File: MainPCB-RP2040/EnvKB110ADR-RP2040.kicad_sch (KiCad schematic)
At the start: 285 parts, among them J2 EVQPU, J5 Conn_01x03_Male, U1 TLV75533PDBVR, U3 RP2040, Y1 3225_4P

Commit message: added missing stabilizers and updated gerber
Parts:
- added stab7, stab8, stab9: MountingHole, Mounting_Keyboard_Stabilizer:Stabilizer_Cherry_MX_2u, symbol Mechanical:MountingHole
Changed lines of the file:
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@@
+    )
+  )
+  (symbol (lib_id "Mechanical:MountingHole") (at 110.49 284.48 0) (unit 1)
+    (in_bom yes) (on_board yes)
+    (property "Reference" "stab8" (id 0) (at 113.03 283.3116 0)
+      (effects (font (size 1.27 1.27)) (justify left))
+    )
+    (property "Value" "MountingHole" (id 1) (at 113.03 285.623 0)
+      (effects (font (size 1.27 1.27)) (justify left))
+    )
+    (property "Footprint" "Mounting_Keyboard_Stabilizer:Stabilizer_Cherry_MX_2u" (id 2) (at 110.49 284.48 0)
+      (effects (font (size 1.27 1.27)) hide)
+    )
+    (property "Datasheet" "~" (id 3) (at 110.49 284.48 0)
+      (effects (font (size 1.27 1.27)) hide)
+    )
+  )
+  (symbol (lib_id "Mechanical:MountingHole") (at 110.49 280.67 0) (unit 1)
+    (in_bom yes) (on_board yes)
+    (property "Reference" "stab7" (id 0) (at 113.03 279.5016 0)
+      (effects (font (size 1.27 1.27)) (justify left))
+    )
+    (property "Value" "MountingHole" (id 1) (at 113.03 281.813 0)
+      (effects (font (size 1.27 1.27)) (justify left))
+    )
+    (property "Footprint" "Mounting_Keyboard_Stabilizer:Stabilizer_Cherry_MX_2u" (id 2) (at 110.49 280.67 0)
+      (effects (font (size 1.27 1.27)) hide)
+    )
+    (property "Datasheet" "~" (id 3) (at 110.49 280.67 0)
+      (effects (font (size 1.27 1.27)) hide)
+    )
+  )
+  (symbol (lib_id "Mechanical:MountingHole") (at 110.49 288.29 0) (unit 1)
+    (in_bom yes) (on_board yes)
+    (property "Reference" "stab9" (id 0) (at 113.03 287.1216 0)
+      (effects (font (size 1.27 1.27)) (justify left))
+    )
+    (property "Value" "MountingHole" (id 1) (at 113.03 289.433 0)
+      (effects (font (size 1.27 1.27)) (justify left))
+    )
+    (property "Footprint" "Mounting_Keyboard_Stabilizer:Stabilizer_Cherry_MX_2u" (id 2) (at 110.49 288.29 0)
+      (effects (font (size 1.27 1.27)) hide)
+    )
+    (property "Datasheet" "~" (id 3) (at 110.49 288.29 0)
+      (effects (font (size 1.27 1.27)) hide)
     )
   )
@@
       (reference "stab6") (unit 1) (value "MountingHole") (footprint "Mounting_Keyboard_Stabilizer:Stabilizer_Cherry_MX_2u")
     )
+    (path "/94062c5c-0205-48cd-835d-0cc87df473b9"
+      (reference "stab7") (unit 1) (value "MountingHole") (footprint "Mounting_Keyboard_Stabilizer:Stabilizer_Cherry_MX_2u")
+    )
+    (path "/88476138-3ded-4644-b39d-e4e08664e937"
+      (reference "stab8") (unit 1) (value "MountingHole") (footprint "Mounting_Keyboard_Stabilizer:Stabilizer_Cherry_MX_2u")
+    )
+    (path "/cfc7fa23-12c8-423d-a92d-1a89c9edd662"
+      (reference "stab9") (unit 1) (value "MountingHole") (footprint "Mounting_Keyboard_Stabilizer:Stabilizer_Cherry_MX_2u")
+    )
   )

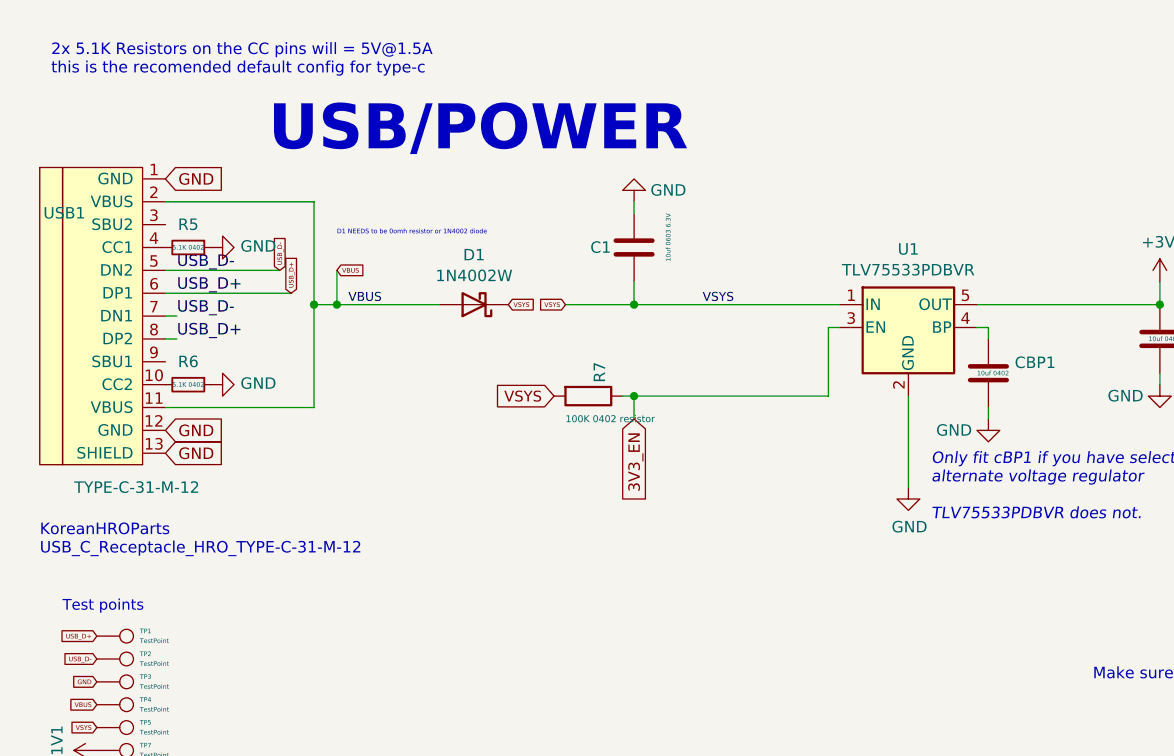
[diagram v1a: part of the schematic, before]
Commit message: swapped port for mid-mount version
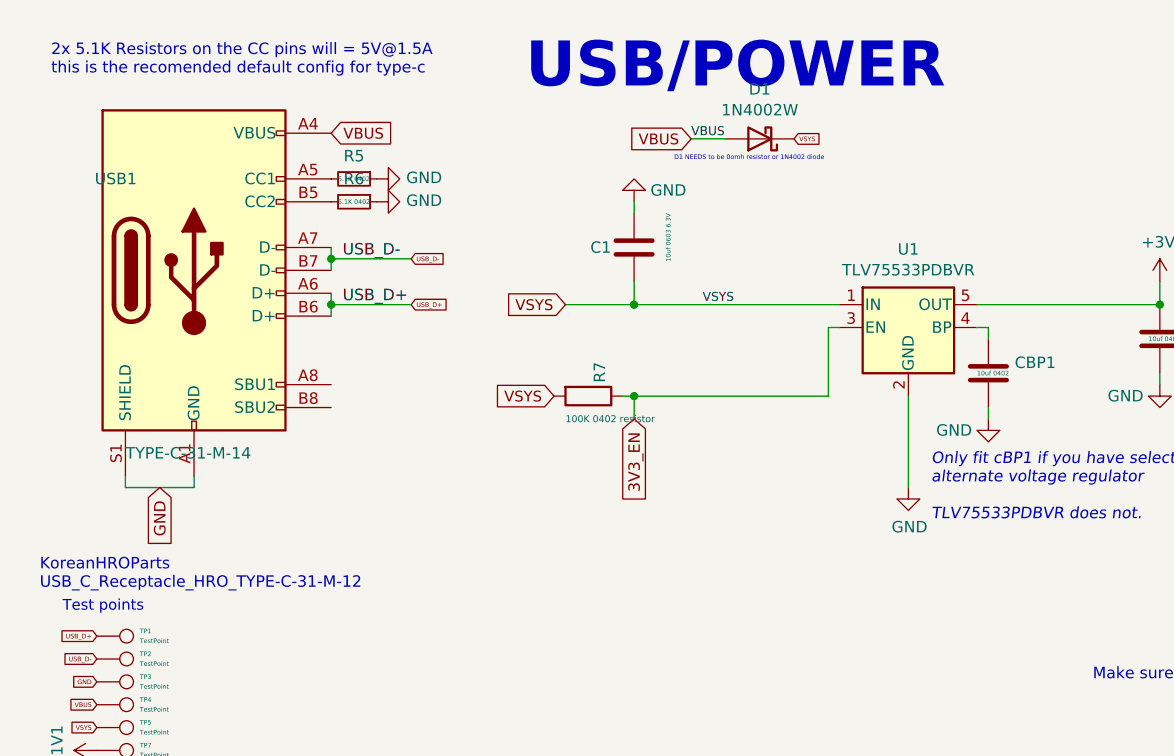
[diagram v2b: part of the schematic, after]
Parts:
- USB1: value TYPE-C-31-M-12 -> TYPE-C-31-M-14; footprint HRO-TYPE-C31-M-12:HRO-TYPE-C-31-M-12 -> josh-connectors:USB_C_TYPE-C-31-M-14; symbol Type-C:HRO-TYPE-C-31-M-12 -> josh-connector:USB_C_U262-161N-4BVC11; LCSC C165948 -> C319148; MPN (none) -> U262-161N-4BVC11; Manufacturer (none) -> XKB Enterprise
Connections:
- net GND: now also USB1.A1 (GND), USB1.A12 (GND), USB1.B1 (GND), USB1.B12 (GND), USB1.S1 (SHIELD); no longer USB1.1 (GND), USB1.12 (GND), USB1.13 (SHIELD)
- net USB_D+: now also USB1.A6 (D+), USB1.B6 (D+); no longer USB1.6 (DP1), USB1.8 (DP2)
- net USB_D-: now also USB1.A7 (D-), USB1.B7 (D-); no longer USB1.5 (DN2), USB1.7 (DN1)
- net VBUS: now also USB1.A4 (VBUS), USB1.A9 (VBUS), USB1.B4 (VBUS), USB1.B9 (VBUS); no longer USB1.11 (VBUS), USB1.2 (VBUS)
- net at R6.2: now also USB1.B5 (CC2); no longer USB1.10 (CC2)
- net at R5.2: now also USB1.A5 (CC1); no longer USB1.4 (CC1)
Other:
- moved on the sheet: D1, R5, R6

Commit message: Added part number for the nor flash and also changed footprint to correct one? also added some smol easter eggs.
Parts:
- FLASH1: value W25Q16 -> W25Q16JVSSIQ; footprint Package_SO:SOIC-8_5.275x5.275mm_P1.27mm -> Package_SO:SOIC-8W_5.3x5.3mm_P1.27mm
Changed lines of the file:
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@@
     (in_bom yes) (on_board yes)
     (property "Reference" "FLASH1" (id 0) (at 78.74 133.35 0))
-    (property "Value" "W25Q16" (id 1) (at 78.74 146.05 0))
-    (property "Footprint" "Package_SO:SOIC-8_5.275x5.275mm_P1.27mm" (id 2) (at 78.74 133.35 0)
+    (property "Value" "W25Q16JVSSIQ" (id 1) (at 78.74 146.05 0))
+    (property "Footprint" "Package_SO:SOIC-8W_5.3x5.3mm_P1.27mm" (id 2) (at 78.74 133.35 0)
       (effects (font (size 1.27 1.27)) (justify left bottom) hide)
     )
@@
     )
     (path "/00000000-0000-0000-0000-0000608edada"
-      (reference "FLASH1") (unit 1) (value "W25Q16") (footprint "Package_SO:SOIC-8_5.275x5.275mm_P1.27mm")
+      (reference "FLASH1") (unit 1) (value "W25Q16JVSSIQ") (footprint "Package_SO:SOIC-8W_5.3x5.3mm_P1.27mm")
     )
     (path "/00000000-0000-0000-0000-000060ccb1e5"

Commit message: various improvements/ made ISO only (for now maybe)
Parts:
- C1: value 10uf 0603 6.3V -> (none); footprint Capacitor_SMD:C_0603_1608Metric -> (none)
- C10, C3: value 1uf 0402 -> (none); footprint Capacitor_SMD:C_0402_1005Metric -> (none)
- C11, C13, C14, C15, C16, C18, C5, C6, C7, C8: value 100nf 0402 -> (none); footprint Capacitor_SMD:C_0402_1005Metric -> (none)
- C17, C4, CBP1: value 10uf 0402 -> (none); footprint Capacitor_SMD:C_0402_1005Metric -> (none)
- C19, C2: value 22pf 0402 -> (none); footprint Capacitor_SMD:C_0402_1005Metric -> (none)
- D1: value 1N4002W -> (none); footprint Diode_SMD:D_SOD-123 -> (none)
- D3: value LED_0603 -> (none); footprint LED_SMD:LED_0603_1608Metric -> (none)
- D_100, D_101, D_102, D_103, D_104, D_105, D_106, D_107, D_108, D_109, D_110, D_111, D_112, D_113, D_114, D_115, D_116, D_12, D_13, D_14, D_15, D_16, D_17, D_18, D_19, D_20, D_21, D_22, D_23, D_24, D_25, D_26, D_27, D_28, D_29, D_30, D_31, D_32, D_33, D_34, D_35, D_36, D_37, D_38, D_39, D_40, D_41, D_42, D_43, D_44, D_45, D_46, D_47, D_48, D_49, D_50, D_51, D_52, D_53, D_54, D_55, D_56, D_57, D_58, D_59, D_60, D_61, D_62, D_63, D_64, D_65, D_66, D_67, D_68, D_69, D_70, D_71, D_72, D_73, D_74, D_75, D_76, D_77, D_78, D_79, D_80, D_81, D_82, D_83, D_84, D_85, D_86, D_87, D_88, D_89, D_90, D_91, D_92, D_93, D_94, D_95, D_96, D_97, D_98, D_99, D_ANSI_1: value SOD-123 -> (none); footprint Diode_SMD:D_SOD-123 -> (none)
- FLASH1: value W25Q16JVSSIQ -> (none); footprint Package_SO:SOIC-8W_5.3x5.3mm_P1.27mm -> (none)
- H1, H10, H11, H12, H13, H14, H15, H16, H17, H18, H2, H3, H4, H5, H6, H7, H8, H9: value MountingHole -> (none); footprint MountingHole:MountingHole_2.2mm_M2_Pad -> (none)
- J2, RSW1: value EVQPU -> (none); footprint Button_Switch_SMD:Panasonic_EVQPUJ_EVQPUA -> (none)
- J5: value Conn_01x03_Male -> (none); footprint Connector_PinHeader_2.54mm:PinHeader_1x03_P2.54mm_Horizontal -> (none)
- K_100, K_101, K_102, K_103, K_104, K_105, K_106, K_107, K_108, K_109, K_110, K_111, K_112, K_113, K_114, K_115, K_116, K_12, K_13, K_14, K_15, K_16, K_17, K_18, K_19, K_20, K_21, K_22, K_23, K_24, K_25, K_26, K_27, K_28, K_29, K_30, K_31, K_32, K_33, K_34, K_35, K_36, K_37, K_38, K_39, K_40, K_41, K_42, K_43, K_44, K_45, K_46, K_47, K_48, K_49, K_50, K_51, K_52, K_53, K_54, K_55, K_56, K_57, K_58, K_59, K_60, K_61, K_62, K_63, K_64, K_65, K_66, K_67, K_68, K_69, K_70, K_71, K_72, K_73, K_74, K_75, K_76, K_77, K_78, K_79, K_80, K_81, K_82, K_83, K_84, K_85, K_86, K_87, K_88, K_89, K_90, K_91, K_92, K_93, K_94, K_95, K_96, K_97, K_98, K_99, K_ANSI_1, K_ANSI_2, K_ANSI_3: value KEYSW -> (none); footprint MX_Only:MXOnly-1U-Hotswap-custom -> (none)
- PWRLED1: value LED_0805 -> (none); footprint LED_SMD:LED_0805_2012Metric -> (none)
- R1, R11: value 1K 0402 Resistor -> (none); footprint Capacitor_SMD:C_0402_1005Metric -> (none)
- R12: value 1K 0402 Resistor -> (none); footprint Resistor_SMD:R_0402_1005Metric -> (none)
- R2: value 10K 0402 -> (none); footprint Capacitor_SMD:C_0402_1005Metric -> (none)
- R3, R4: value 27 0402 Resistor -> (none); footprint Resistor_SMD:R_0402_1005Metric -> (none)
- R5, R6: value 5.1K 0402 -> (none); footprint Resistor_SMD:R_0402_1005Metric -> (none)
- R7: value 100K 0402 resistor -> (none); footprint Resistor_SMD:R_0402_1005Metric -> (none)
- R8: value 470 0402 Resistor -> (none); footprint Resistor_SMD:R_0402_1005Metric -> (none)
- TP1, TP2, TP3, TP4, TP5, TP6, TP7, TP8: value TestPoint -> (none); footprint TestPoint:TestPoint_Pad_D1.0mm -> (none)
- U1: value TLV75533PDBVR -> (none); footprint Package_TO_SOT_SMD:SOT-23-5 -> (none)
- U3: value RP2040 -> (none); footprint RP2040_minimal:RP2040-QFN-56 -> (none)
- USB1: value TYPE-C-31-M-14 -> (none); footprint josh-connectors:USB_C_TYPE-C-31-M-14 -> (none)
- Y1: value 3225_4P -> (none); footprint Crystal:Crystal_SMD_3225-4Pin_3.2x2.5mm -> (none)
- stab1, stab2, stab3, stab4, stab6, stab7, stab8, stab9: value MountingHole -> (none); footprint Mounting_Keyboard_Stabilizer:Stabilizer_Cherry_MX_2u -> (none)
- stab5: value MountingHole -> (none); footprint Mounting_Keyboard_Stabilizer:Stabilizer_Cherry_MX_6.25u -> (none)

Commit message: properly implemented ANSI/ISO support.
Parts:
- C1: value (none) -> 10uf 0603 6.3V; footprint (none) -> Capacitor_SMD:C_0603_1608Metric
- C10, C3: value (none) -> 1uf 0402; footprint (none) -> Capacitor_SMD:C_0402_1005Metric
- C11, C13, C14, C15, C16, C18, C5, C6, C7, C8: value (none) -> 100nf 0402; footprint (none) -> Capacitor_SMD:C_0402_1005Metric
- C17, C4, CBP1: value (none) -> 10uf 0402; footprint (none) -> Capacitor_SMD:C_0402_1005Metric
- C19, C2: value (none) -> 22pf 0402; footprint (none) -> Capacitor_SMD:C_0402_1005Metric
- D1: value (none) -> 1N4002W; footprint (none) -> Diode_SMD:D_SOD-123
- D3: value (none) -> LED_0603; footprint (none) -> LED_SMD:LED_0603_1608Metric
- D_100, D_101, D_102, D_103, D_104, D_105, D_106, D_107, D_108, D_109, D_110, D_111, D_112, D_113, D_114, D_115, D_116, D_12, D_13, D_14, D_15, D_16, D_17, D_18, D_19, D_20, D_21, D_22, D_23, D_24, D_25, D_26, D_27, D_28, D_29, D_30, D_31, D_32, D_33, D_34, D_35, D_36, D_37, D_38, D_39, D_40, D_41, D_42, D_43, D_44, D_45, D_46, D_47, D_48, D_49, D_50, D_51, D_52, D_53, D_54, D_55, D_56, D_57, D_58, D_59, D_60, D_61, D_62, D_63, D_64, D_65, D_66, D_67, D_68, D_69, D_70, D_71, D_72, D_73, D_74, D_75, D_76, D_77, D_78, D_79, D_80, D_81, D_82, D_83, D_84, D_85, D_86, D_87, D_88, D_89, D_90, D_91, D_92, D_93, D_94, D_95, D_96, D_97, D_98, D_99, D_ANSI_1: value (none) -> SOD-123; footprint (none) -> Diode_SMD:D_SOD-123
- FLASH1: value (none) -> W25Q16JVSSIQ; footprint (none) -> Package_SO:SOIC-8W_5.3x5.3mm_P1.27mm
- H1, H10, H11, H12, H13, H14, H15, H16, H17, H18, H2, H3, H4, H5, H6, H7, H8, H9: value (none) -> MountingHole; footprint (none) -> MountingHole:MountingHole_2.2mm_M2_Pad
- J2, RSW1: value (none) -> EVQPU; footprint (none) -> Button_Switch_SMD:Panasonic_EVQPUJ_EVQPUA
- J5: value (none) -> Conn_01x03_Male; footprint (none) -> Connector_PinHeader_2.54mm:PinHeader_1x03_P2.54mm_Horizontal
- K_100, K_101, K_102, K_103, K_104, K_105, K_106, K_107, K_108, K_109, K_110, K_111, K_112, K_113, K_114, K_115, K_116, K_12, K_13, K_14, K_15, K_16, K_17, K_18, K_19, K_20, K_21, K_22, K_23, K_24, K_25, K_26, K_27, K_28, K_29, K_30, K_31, K_32, K_33, K_34, K_35, K_36, K_37, K_38, K_39, K_40, K_41, K_42, K_43, K_44, K_45, K_46, K_47, K_48, K_49, K_50, K_51, K_52, K_53, K_54, K_55, K_56, K_57, K_58, K_59, K_60, K_61, K_62, K_63, K_64, K_65, K_66, K_67, K_68, K_69, K_70, K_71, K_72, K_73, K_74, K_75, K_76, K_77, K_78, K_79, K_80, K_81, K_82, K_83, K_84, K_85, K_86, K_87, K_88, K_89, K_90, K_91, K_92, K_93, K_94, K_95, K_96, K_97, K_98, K_99, K_ANSI_1, K_ANSI_2, K_ANSI_3: value (none) -> KEYSW; footprint (none) -> EnvExtras:MXOnly-1U-Hotswap-Modified
- PWRLED1: value (none) -> LED_0805; footprint (none) -> LED_SMD:LED_0805_2012Metric
- R1, R11: value (none) -> 1K 0402 Resistor; footprint (none) -> Capacitor_SMD:C_0402_1005Metric
- R12: value (none) -> 1K 0402 Resistor; footprint (none) -> Resistor_SMD:R_0402_1005Metric
- R2: value (none) -> 10K 0402; footprint (none) -> Capacitor_SMD:C_0402_1005Metric
- R3, R4: value (none) -> 27 0402 Resistor; footprint (none) -> Resistor_SMD:R_0402_1005Metric
- R5, R6: value (none) -> 5.1K 0402; footprint (none) -> Resistor_SMD:R_0402_1005Metric
- R7: value (none) -> 100K 0402 resistor; footprint (none) -> Resistor_SMD:R_0402_1005Metric
- R8: value (none) -> 470 0402 Resistor; footprint (none) -> Resistor_SMD:R_0402_1005Metric
- TP1, TP2, TP3, TP4, TP5, TP6, TP7, TP8: value (none) -> TestPoint; footprint (none) -> TestPoint:TestPoint_Pad_D1.0mm
- U1: value (none) -> TLV75533PDBVR; footprint (none) -> Package_TO_SOT_SMD:SOT-23-5
- U3: value (none) -> RP2040; footprint (none) -> RP2040_minimal:RP2040-QFN-56
- USB1: value (none) -> TYPE-C-31-M-14; footprint (none) -> josh-connectors:USB_C_TYPE-C-31-M-14
- Y1: value (none) -> 3225_4P; footprint (none) -> Crystal:Crystal_SMD_3225-4Pin_3.2x2.5mm
- stab1, stab2, stab3, stab4, stab6, stab7, stab8, stab9: value (none) -> MountingHole; footprint (none) -> Mounting_Keyboard_Stabilizer:Stabilizer_Cherry_MX_2u
- stab5: value (none) -> MountingHole; footprint (none) -> Mounting_Keyboard_Stabilizer:Stabilizer_Cherry_MX_6.25u
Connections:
- net GND: no longer H1.1, H10.1, H11.1, H12.1, H13.1, H14.1, H15.1, H16.1, H17.1, H18.1, H2.1, H3.1, H4.1, H5.1, H6.1, H7.1, H8.1, H9.1

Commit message: various updates and adjustments
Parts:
- removed TP2, TP3, TP4, TP5, TP6, TP7, TP8: TestPoint, TestPoint:TestPoint_Pad_D1.0mm, symbol Connector:TestPoint
- added C12, C20, C9: 100nf 0402, Capacitor_SMD:C_0402_1005Metric, symbol Device:C
- added D2, D4, D5: WS2812B, LED_SMD:LED_WS2812B_PLCC4_5.0x5.0mm_P3.2mm, symbol LED:WS2812B
- D3: value LED_0603 -> LED_0805; footprint LED_SMD:LED_0603_1608Metric -> LED_SMD:LED_0805_2012Metric
- TP1: footprint TestPoint:TestPoint_Pad_D1.0mm -> TestPoint:TestPoint_Pad_4.0x4.0mm; LCSC (none) -> (none)
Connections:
- net GND: now also C12.1, C20.1, C9.1, D2.3 (VSS), D4.3 (VSS), D5.3 (VSS)
- net GPIO0: now also D2.4 (DIN)
- net USB_D+: no longer TP1.1
- net VBUS: now also C12.2, C20.2, C9.2, D2.1 (VDD), D4.1 (VDD), D5.1 (VDD)
- new net: D5.2 (DOUT), TP1.1
- new net: D4.2 (DOUT), D5.4 (DIN)
- new net: D2.2 (DOUT), D4.4 (DIN)
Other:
- note removed: "Test points"
- note removed: "place one by the CPU and one by the regulator (3.3V Test points)"
